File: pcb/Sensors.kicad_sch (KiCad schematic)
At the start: 8 parts, among them IC2 SHT35-DIS-B2.5KS, U10 DPS368XTSA1

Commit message: in works
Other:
- note added: "co2 sensor, not integrated"
- company: (none) -> Infineon Technologies
- title: (none) -> SensEdu 0.9
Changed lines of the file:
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@@
 	(generator_version "9.0")
 	(paper "A4")
+	(title_block
+		(title "SensEdu 0.9")
+		(date "2025-12-05")
+		(company "Infineon Technologies")
+		(comment 1 "Author: Arshad Pattathil/Harald Gietler/Azra Talic/Felix Ober")
+	)
 	(rectangle
 		(start 22.86 26.67)
@@
 			)
 		)
+	)
+	(text "co2 sensor, not integrated"
+		(exclude_from_sim no)
+		(at 125.73 102.87 0)
+		(effects
+			(font
+				(size 1.27 1.27)
+			)
+		)

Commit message: fix: PCB final fixes
Added simulation for dc offset after ac coupling
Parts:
- renumbered C56 to C58, C57 to C59
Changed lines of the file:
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@@
 		(on_board yes)
 		(dnp no)
-		(property "Reference" "C57"
+		(property "Reference" "C59"
 			(at 193.04 35.56 90)
 			(effects
@@
 			(project "SensEdu"
 				(path "/e63e39d7-6ac0-4ffd-8aa3-1841a4541b55/d6e506e4-1660-4f12-9b07-0782300f1012"
-					(reference "C57")
+					(reference "C59")
 					(unit 1)
 				)
@@
 		(on_board yes)
 		(dnp no)
-		(property "Reference" "C56"
+		(property "Reference" "C58"
 			(at 113.03 58.42 0)
 			(effects
@@
 			(project "SensEdu"
 				(path "/e63e39d7-6ac0-4ffd-8aa3-1841a4541b55/d6e506e4-1660-4f12-9b07-0782300f1012"
-					(reference "C56")
+					(reference "C58")
 					(unit 1)
 				)

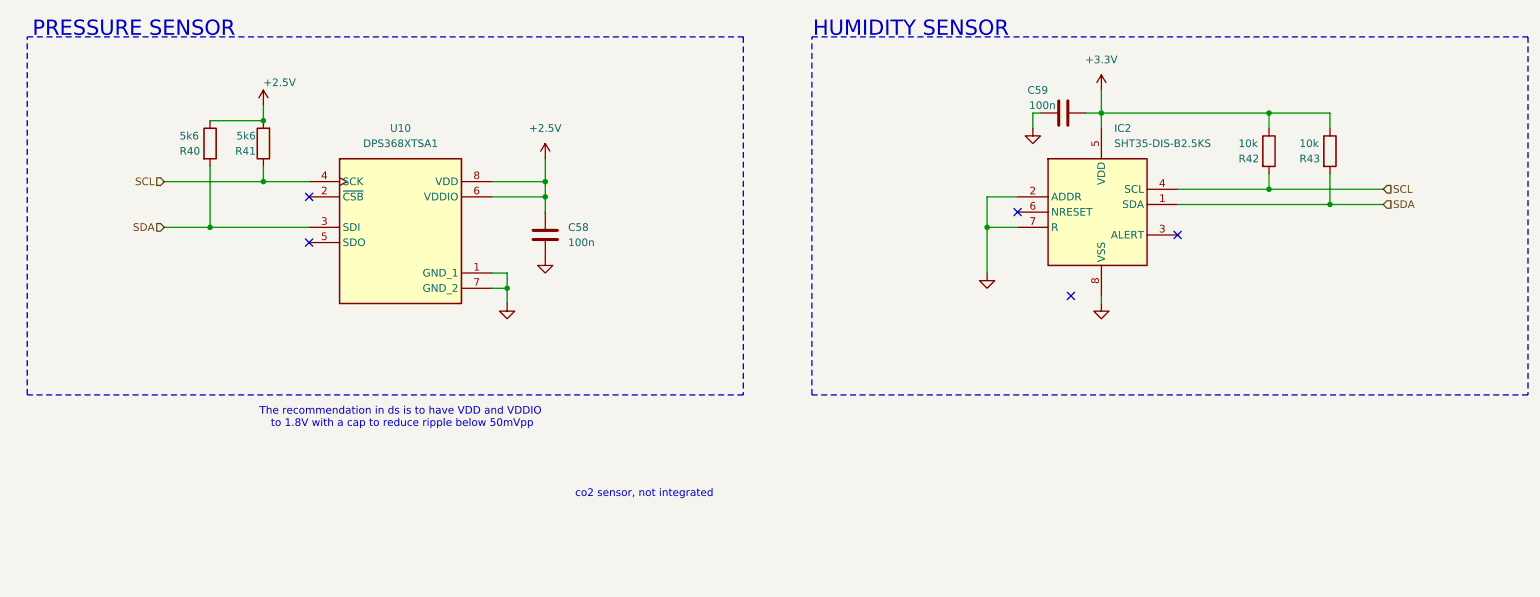
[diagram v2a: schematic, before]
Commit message: feat: Redraw PCB layout
- Change supply polarity and pin numbers of ADA4511
- Change cap of switches to 100n to reduce bom
- Change supply of sensors to unison 3.3V
- Rearrange mic and amps pins
- Add mountains
- Add Infineon logo
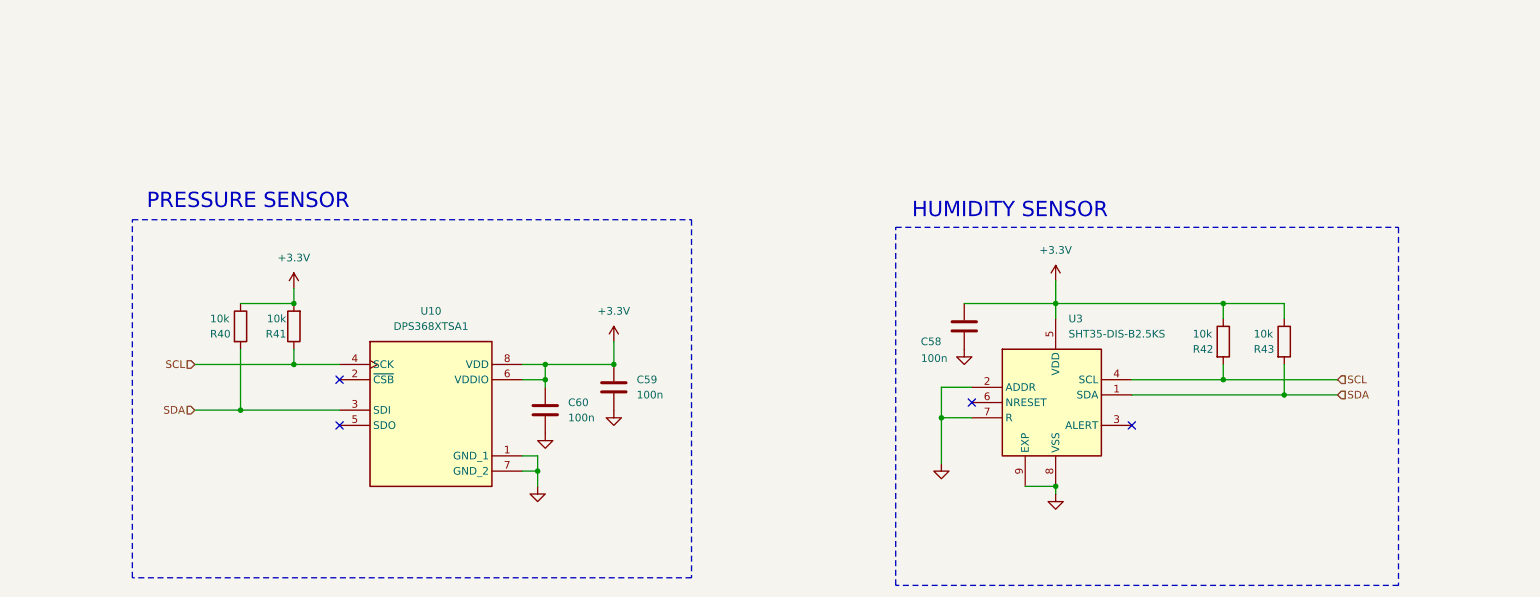
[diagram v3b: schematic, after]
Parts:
- removed IC2: SHT35-DIS-B2.5KS, SensEdu:SHT35-DIS-B2.5KS, symbol SensEdu:SHT35-DIS-B2.5KS
- added C59: 100n, Capacitor_SMD:C_0603_1608Metric, symbol SensEdu:C
- added U3: SHT35-DIS-B2.5KS, SensEdu:SHT35-DIS-B2.5KS, symbol SensEdu:SHT35-DIS-B2.5KS
- C58: renamed from C59; footprint Capacitor_SMD:C_0805_2012Metric -> Capacitor_SMD:C_0603_1608Metric; symbol Device:C -> SensEdu:C
- C60: renamed from C58; footprint Capacitor_SMD:C_0805_2012Metric -> Capacitor_SMD:C_0603_1608Metric; symbol Device:C -> SensEdu:C
- R40, R41: value 5k6 -> 10k; footprint Resistor_SMD:R_0805_2012Metric -> Resistor_SMD:R_0603_1608Metric; symbol Device:R -> SensEdu:R
- R42, R43: footprint Resistor_SMD:R_0805_2012Metric -> Resistor_SMD:R_0603_1608Metric; symbol Device:R -> SensEdu:R
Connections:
- net +2.5V is gone; now on net +3.3V: C60.1, R40.1, R41.2, U10.6 (VDDIO), U10.8 (VDD)
- net +3.3V: now also C59.1, U3.5 (VDD)
- net GND: now also C59.2, U3.2 (ADDR), U3.7 (R), U3.8 (VSS), U3.9 (EXP)
- net SCL: now also U3.4 (SCL)
- net SDA: now also U3.1 (SDA)
- no-connect marks 5 -> 4
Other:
- note removed: "The recommendation in ds is to have VDD and VDDIO to 1.8V with a cap to reduce ripple below 50mVpp"
- note removed: "co2 sensor, not integrated"
- moved on the sheet: C58, C60, R40, R41, R42, R43, U10

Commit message: refactor: Update PDF and information
- Add BOM
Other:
- title: SensEdu 0.9 -> SensEdu
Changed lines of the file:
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@@
 	(paper "A4")
 	(title_block
-		(title "SensEdu 0.9")
-		(date "2025-12-05")
+		(title "SensEdu")
+		(date "2026-02-26")
 		(rev "0.9")
 		(company "Infineon Technologies")

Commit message: feat: Improve PCB design after tests of rev 0.8
- Added new generation of humidity sensor
- New silkscreen information for different components
- Added additional testpoints
- Removed PWM path for ultrasound transmitter
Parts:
- removed U3: SHT35-DIS-B2.5KS, SensEdu:SHT35-DIS-B2.5KS, symbol SensEdu:SHT35-DIS-B2.5KS
- added U10: SHT40-AD1F-R2, SensEdu:SHT40AD1FR2, symbol SensEdu:SHT40-AD1F-R2
- C58, C59, C60: footprint Capacitor_SMD:C_0603_1608Metric -> SensEdu:C_0603_1608Metric
- R40, R41, R42, R43: footprint Resistor_SMD:R_0603_1608Metric -> SensEdu:R_0603_1608Metric
- renumbered U10 to U9
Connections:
- net +3.3V: now also U10.3 (VDD)
- net GND: now also U10.4 (VSS)
- net SCL: now also U10.2 (SCL)
- net SDA: now also U10.1 (SDA)
- no-connect marks 4 -> 2
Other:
- note added: "Sensor has hole for air contact which should not be confused with the dot on the package for orientation indication"
- moved on the sheet: C58, R42, R43
